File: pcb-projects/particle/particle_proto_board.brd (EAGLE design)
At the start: 33.7 x 30.5 mm, 35 parts, among them IC1 ATTINY20-MMH, IC2 DMC2400V, IC3 DMC2400V, SW1 T/S-PI SW, SW2 T/S-PI SW, SW3 T/S-PI SW

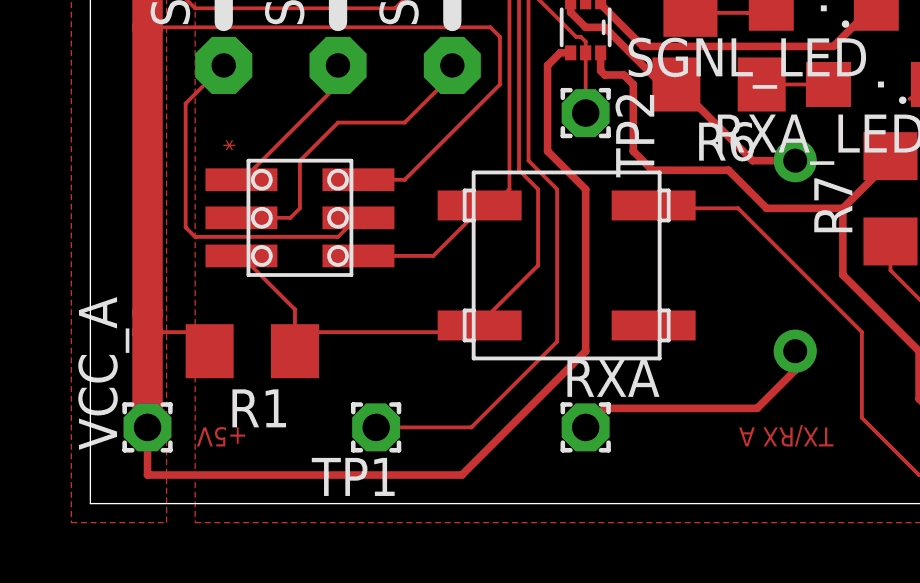
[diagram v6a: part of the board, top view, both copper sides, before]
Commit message: enhanced switch: now has 4 terminals - polygon filling now makes termal pad correct
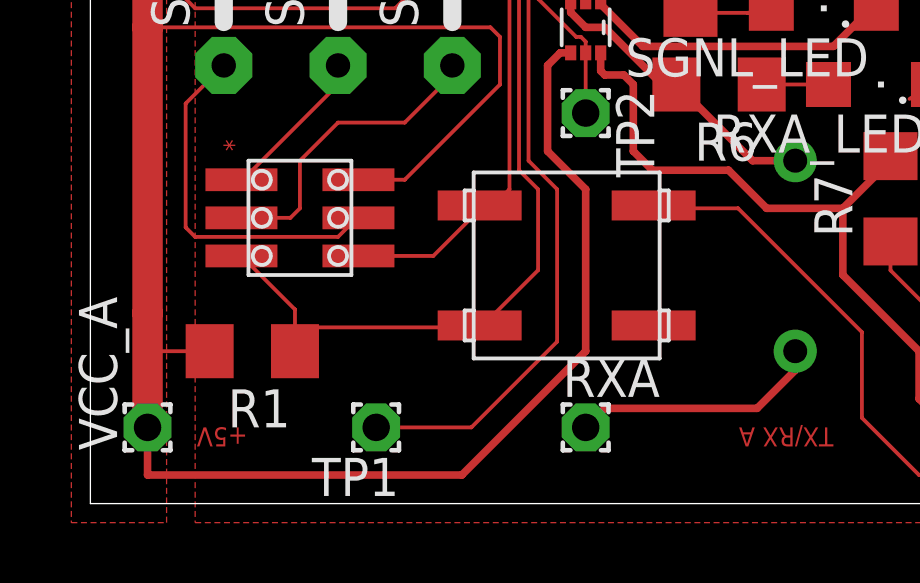
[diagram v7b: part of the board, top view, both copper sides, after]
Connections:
- net GND: now also S2.1@1, S2.1@2; no longer S2.1
- net RESET: now also S2.2@1; no longer S2.2
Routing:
- net RESET: track 44.1 -> 44.8 mm
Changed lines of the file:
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@@
 <setting verticaltext="up"/>
 </settings>
-<grid distance="12.5" unitdist="mil" unit="mil" style="lines" multiple="1" display="yes" altdistance="0.00625" altunitdist="inch" altunit="inch"/>
+<grid distance="6.25" unitdist="mil" unit="mil" style="lines" multiple="1" display="yes" altdistance="0.00625" altunitdist="inch" altunit="inch"/>
 <layers>
 <layer number="1" name="Top" color="4" fill="1" visible="yes" active="yes"/>
@@
 <wire x1="14.125" y1="26.035" x2="13.97" y2="26.035" width="0.127" layer="1"/>
 <wire x1="13.97" y1="26.035" x2="13.97" y2="25.4" width="0.127" layer="1"/>
-<contactref element="S2" pad="1"/>
+<contactref element="S2" pad="1@1"/>
 <wire x1="31.75" y1="2.54" x2="31.75" y2="1.905" width="0.127" layer="1"/>
 <wire x1="31.75" y1="1.905" x2="30.7975" y2="0.9525" width="0.127" layer="1"/>
@@
 <wire x1="13.97" y1="10.4775" x2="13.97" y2="18.7325" width="0.127" layer="1"/>
 <wire x1="25.7175" y1="5.715" x2="21.59" y2="9.8425" width="0.127" layer="1"/>
-<wire x1="21.59" y1="9.8425" x2="18.7325" y2="9.8425" width="0.127" layer="1"/>
 <wire x1="26.035" y1="16.51" x2="26.035" y2="17.78" width="0.254" layer="1"/>
 <wire x1="26.035" y1="17.78" x2="26.9875" y2="18.7325" width="0.254" layer="1"/>
@@
 <wire x1="13.0175" y1="9.8425" x2="11.43" y2="8.255" width="0.127" layer="1"/>
 <wire x1="13.335" y1="9.8425" x2="13.97" y2="10.4775" width="0.127" layer="1"/>
+<contactref element="S2" pad="1@2"/>
+<wire x1="18.7325" y1="10.00125" x2="18.89125" y2="9.8425" width="0.127" layer="1"/>
+<wire x1="18.89125" y1="9.8425" x2="21.59" y2="9.8425" width="0.127" layer="1"/>
 <wire x1="17.01" y1="16.725" x2="13.97" y2="18.7325" width="0" layer="19" extent="1-1"/>
 <wire x1="22.86" y1="19.685" x2="26.035" y2="17.78" width="0" layer="19" extent="1-1"/>
@@
 <wire x1="12.7" y1="20.6375" x2="14.2875" y2="19.05" width="0.127" layer="1"/>
 <wire x1="14.2875" y1="19.05" x2="14.2875" y2="11.1125" width="0.127" layer="1"/>
-<contactref element="S2" pad="2"/>
+<contactref element="S2" pad="2@1"/>
 <wire x1="14.2875" y1="11.1125" x2="14.9225" y2="10.4775" width="0.127" layer="1"/>
 <contactref element="TPI/SPI" pad="5"/>
-<wire x1="12.7" y1="5.715" x2="14.9225" y2="7.9375" width="0.127" layer="1"/>
-<wire x1="14.9225" y1="7.9375" x2="14.9225" y2="10.4775" width="0.127" layer="1"/>
-<wire x1="6.985" y1="5.715" x2="12.7" y2="5.715" width="0.127" layer="1"/>
+<wire x1="14.9225" y1="7.77875" x2="14.9225" y2="10.4775" width="0.127" layer="1"/>
 <wire x1="5.035" y1="8.255" x2="6.8195" y2="6.4705" width="0.127" layer="1"/>
 <wire x1="6.8195" y1="6.4705" x2="6.8195" y2="5.08" width="0.127" layer="1"/>
-<wire x1="12.7" y1="5.715" x2="12.975" y2="5.9375" width="0" layer="19" extent="1-1"/>
-<wire x1="6.8195" y1="5.08" x2="6.985" y2="5.715" width="0" layer="19" extent="1-1"/>
+<wire x1="13.0175" y1="5.87375" x2="14.9225" y2="7.77875" width="0.127" layer="1"/>
+<wire x1="13.0175" y1="5.87375" x2="7.3025" y2="5.87375" width="0.127" layer="1"/>
+<wire x1="7.3025" y1="5.87375" x2="6.82625" y2="5.3975" width="0.127" layer="1"/>
+<wire x1="6.82625" y1="5.3975" x2="6.82625" y2="5.08" width="0.127" layer="1"/>
+<wire x1="13.0175" y1="5.87375" x2="12.975" y2="5.9375" width="0" layer="19" extent="1-1"/>
+<wire x1="6.8195" y1="5.08" x2="6.82625" y2="5.08" width="0" layer="19" extent="1-1"/>
 </signal>
 <signal name="RX_B" class="1">
@@
 <wire x1="1.905" y1="25.7175" x2="1.905" y2="15.875" width="1.016" layer="1"/>
 <wire x1="1.905" y1="15.875" x2="1.905" y2="6.35" width="1.016" layer="1"/>
-<wire x1="1.905" y1="6.35" x2="1.905" y2="5.715" width="1.016" layer="1"/>
-<wire x1="1.905" y1="5.715" x2="1.905" y2="2.54" width="1.016" layer="1"/>
+<wire x1="1.905" y1="6.35" x2="1.905" y2="2.54" width="1.016" layer="1"/>
 <wire x1="15.24" y1="14.605" x2="15.24" y2="11.7475" width="0.254" layer="1"/>
 <wire x1="15.24" y1="11.7475" x2="16.51" y2="10.4775" width="0.254" layer="1"/>
@@
 <wire x1="13.6525" y1="15.5575" x2="13.335" y2="15.875" width="0.127" layer="1"/>
 <wire x1="13.335" y1="15.875" x2="1.905" y2="15.875" width="0.127" layer="1"/>
-<wire x1="4.1275" y1="5.715" x2="1.905" y2="5.715" width="0.127" layer="1"/>
 <wire x1="27.46375" y1="25.4" x2="26.67" y2="26.19375" width="0.254" layer="1"/>
 <wire x1="1.905" y1="0.9525" x2="12.3825" y2="0.9525" width="0.254" layer="1"/>
 <wire x1="1.905" y1="0.9525" x2="1.905" y2="2.54" width="0.254" layer="1"/>
+<wire x1="4.1275" y1="5.08" x2="1.5875" y2="5.08" width="0.127" layer="1"/>
 <wire x1="16.06" y1="24.2625" x2="20.32" y2="26.67" width="0" layer="19" extent="1-1"/>
-<wire x1="3.9755" y1="5.08" x2="4.1275" y2="5.715" width="0" layer="19" extent="1-1"/>
+<wire x1="3.9755" y1="5.08" x2="4.1275" y2="5.08" width="0" layer="19" extent="1-1"/>
 </signal>
 <signal name="TX_B">

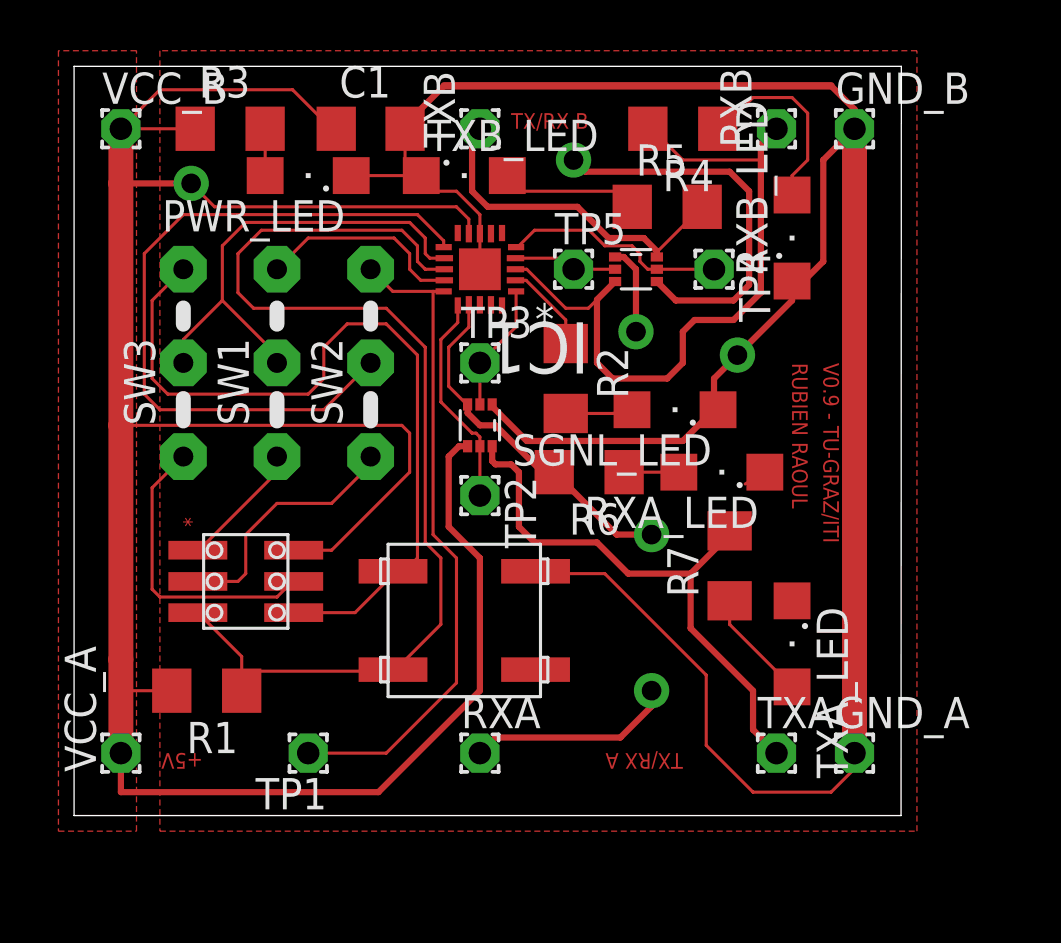
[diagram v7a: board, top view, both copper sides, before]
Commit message: successfully connected four tiny airwires below pads
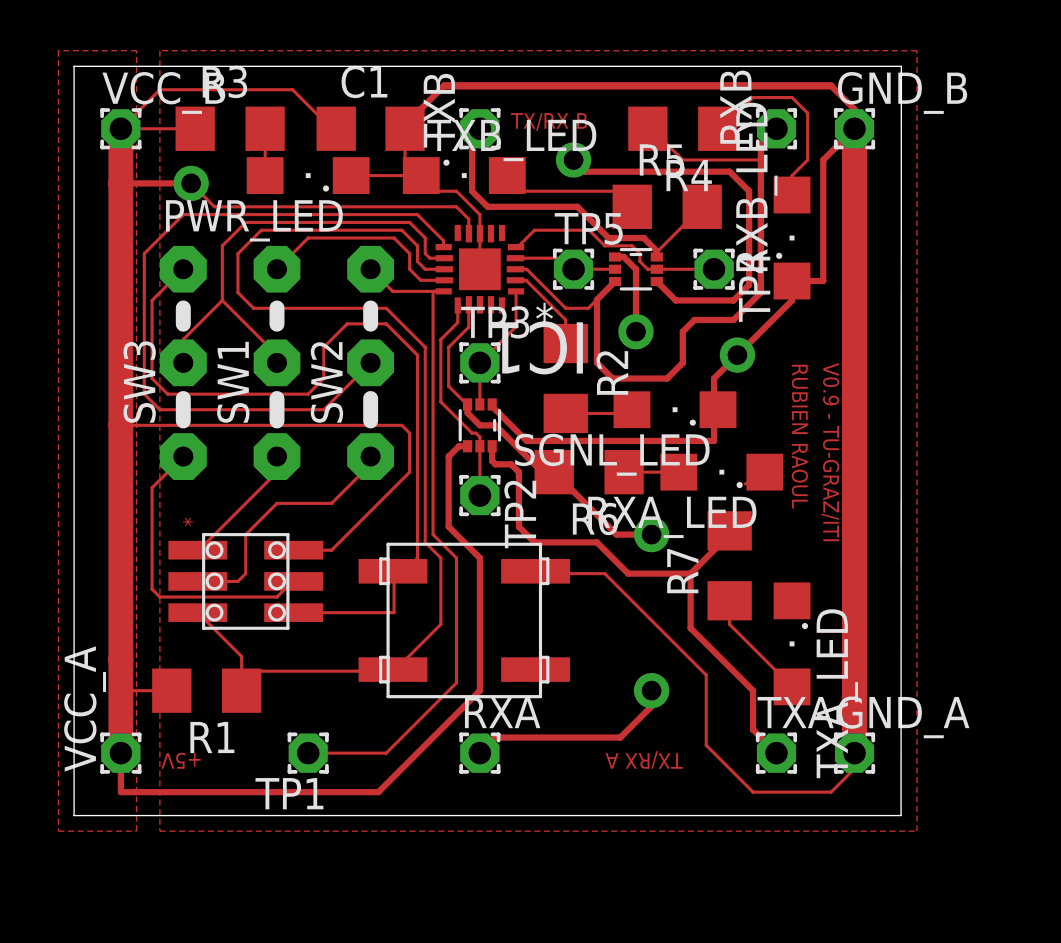
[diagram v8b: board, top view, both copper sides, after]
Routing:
- net GND: track 138.2 -> 140.3 mm
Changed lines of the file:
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@@
 <layers>
 <layer number="1" name="Top" color="4" fill="1" visible="yes" active="yes"/>
-<layer number="16" name="Bottom" color="1" fill="1" visible="yes" active="yes"/>
-<layer number="17" name="Pads" color="2" fill="1" visible="yes" active="yes"/>
-<layer number="18" name="Vias" color="2" fill="1" visible="yes" active="yes"/>
+<layer number="16" name="Bottom" color="1" fill="1" visible="no" active="yes"/>
+<layer number="17" name="Pads" color="2" fill="1" visible="no" active="yes"/>
+<layer number="18" name="Vias" color="2" fill="1" visible="no" active="yes"/>
 <layer number="19" name="Unrouted" color="6" fill="1" visible="yes" active="yes"/>
-<layer number="20" name="Dimension" color="15" fill="1" visible="yes" active="yes"/>
+<layer number="20" name="Dimension" color="15" fill="1" visible="no" active="yes"/>
 <layer number="21" name="tPlace" color="7" fill="1" visible="no" active="yes"/>
 <layer number="22" name="bPlace" color="7" fill="1" visible="no" active="yes"/>
@@
 <wire x1="31.75" y1="27.94" x2="30.48" y2="26.67" width="0.254" layer="1"/>
 <wire x1="29.21" y1="21.745" x2="29.6825" y2="21.2725" width="0.127" layer="1"/>
-<wire x1="30.48" y1="26.67" x2="30.48" y2="22.5425" width="0.254" layer="1"/>
-<wire x1="30.48" y1="22.5425" x2="29.6825" y2="21.745" width="0.254" layer="1"/>
+<wire x1="30.48" y1="26.67" x2="30.48" y2="21.74875" width="0.254" layer="1"/>
+<wire x1="30.48" y1="21.74875" x2="29.6825" y2="21.745" width="0.254" layer="1"/>
 <wire x1="29.6825" y1="21.745" x2="29.21" y2="21.745" width="0.254" layer="1"/>
-<wire x1="24.765" y1="15.24" x2="18.415" y2="15.24" width="0.254" layer="1"/>
-<wire x1="24.765" y1="15.24" x2="26.035" y2="16.51" width="0.254" layer="1"/>
+<wire x1="26.035" y1="15.24" x2="18.415" y2="15.24" width="0.254" layer="1"/>
 <wire x1="28.1025" y1="13.97" x2="27.305" y2="13.49" width="0.127" layer="1"/>
 <wire x1="31.75" y1="27.94" x2="31.75" y2="2.54" width="1.016" layer="1"/>
@@
 <wire x1="13.97" y1="10.4775" x2="13.97" y2="18.7325" width="0.127" layer="1"/>
 <wire x1="25.7175" y1="5.715" x2="21.59" y2="9.8425" width="0.127" layer="1"/>
-<wire x1="26.035" y1="16.51" x2="26.035" y2="17.78" width="0.254" layer="1"/>
+<wire x1="26.035" y1="15.24" x2="26.035" y2="17.78" width="0.254" layer="1"/>
 <wire x1="26.035" y1="17.78" x2="26.9875" y2="18.7325" width="0.254" layer="1"/>
-<wire x1="8.89" y1="8.255" x2="11.43" y2="8.255" width="0.127" layer="1"/>
+<wire x1="8.89" y1="8.255" x2="13.0175" y2="8.255" width="0.127" layer="1"/>
 <wire x1="13.335" y1="9.8425" x2="13.0175" y2="9.8425" width="0.127" layer="1"/>
-<wire x1="13.0175" y1="9.8425" x2="11.43" y2="8.255" width="0.127" layer="1"/>
+<wire x1="13.0175" y1="9.8425" x2="13.0175" y2="8.255" width="0.127" layer="1"/>
 <wire x1="13.335" y1="9.8425" x2="13.97" y2="10.4775" width="0.127" layer="1"/>
 <contactref element="S2" pad="1@2"/>
@@
 <wire x1="7.3025" y1="5.87375" x2="6.82625" y2="5.3975" width="0.127" layer="1"/>
 <wire x1="6.82625" y1="5.3975" x2="6.82625" y2="5.08" width="0.127" layer="1"/>
-<wire x1="13.0175" y1="5.87375" x2="12.975" y2="5.9375" width="0" layer="19" extent="1-1"/>
-<wire x1="6.8195" y1="5.08" x2="6.82625" y2="5.08" width="0" layer="19" extent="1-1"/>
+<wire x1="12.975" y1="5.9375" x2="13.0175" y2="5.9375" width="0.127" layer="1"/>
+<wire x1="13.0175" y1="5.9375" x2="13.0175" y2="5.87375" width="0.127" layer="1"/>
+<wire x1="6.82625" y1="5.08" x2="6.8195" y2="5.08" width="0" layer="19" extent="1-1"/>
 </signal>
 <signal name="RX_B" class="1">
@@
 <wire x1="5.08" y1="10.795" x2="8.255" y2="13.97" width="0.127" layer="1"/>
 <wire x1="8.255" y1="13.97" x2="8.255" y2="14.605" width="0.127" layer="1"/>
-<wire x1="5.035" y1="10.795" x2="5.08" y2="10.795" width="0" layer="19" extent="1-1"/>
+<wire x1="5.035" y1="10.795" x2="5.08" y2="10.795" width="0.127" layer="1"/>
 </signal>
 <signal name="N$18">
@@
 <wire x1="3.175" y1="9.2075" x2="3.175" y2="13.335" width="0.127" layer="1"/>
 <wire x1="3.175" y1="13.335" x2="4.445" y2="14.605" width="0.127" layer="1"/>
-<wire x1="8.89" y1="9.525" x2="8.935" y2="9.525" width="0" layer="19" extent="1-1"/>
+<wire x1="8.89" y1="9.525" x2="8.935" y2="9.525" width="0.127" layer="1"/>
 </signal>
 <signal name="N$11">
-<wire x1="5.08" y1="9.525" x2="6.6675" y2="9.525" width="0.127" layer="1"/>
+<wire x1="5.035" y1="9.525" x2="6.6675" y2="9.525" width="0.127" layer="1"/>
 <wire x1="6.6675" y1="9.525" x2="6.985" y2="9.8425" width="0.127" layer="1"/>
 <wire x1="6.985" y1="9.8425" x2="6.985" y2="11.43" width="0.127" layer="1"/>
@@
 <wire x1="10.4775" y1="12.7" x2="12.065" y2="14.2875" width="0.127" layer="1"/>
 <wire x1="12.065" y1="14.2875" x2="12.065" y2="14.605" width="0.127" layer="1"/>
-<wire x1="5.035" y1="9.525" x2="5.08" y2="9.525" width="0" layer="19" extent="1-1"/>
 </signal>
 </signals>
